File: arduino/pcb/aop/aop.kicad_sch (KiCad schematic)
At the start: 11 parts, among them J1 Conn_01x02_Pin, Q1 AO4435, SW1 SW_Push, SW2 SW_Push, U1 ESP32-C3_SUPERMINI_TH

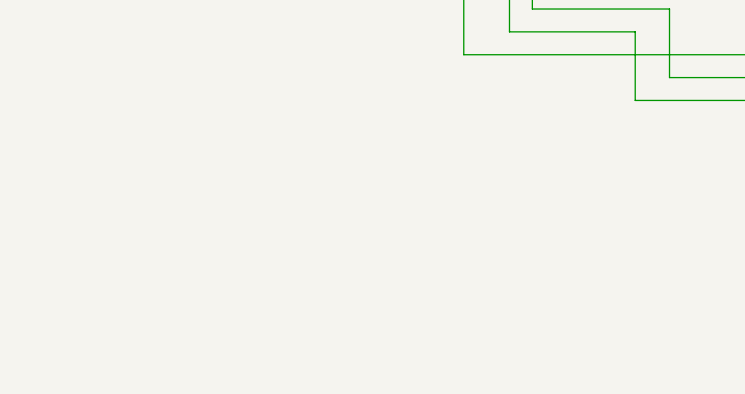
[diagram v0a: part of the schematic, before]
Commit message: [pcb] Stabilize power rail with capacitors
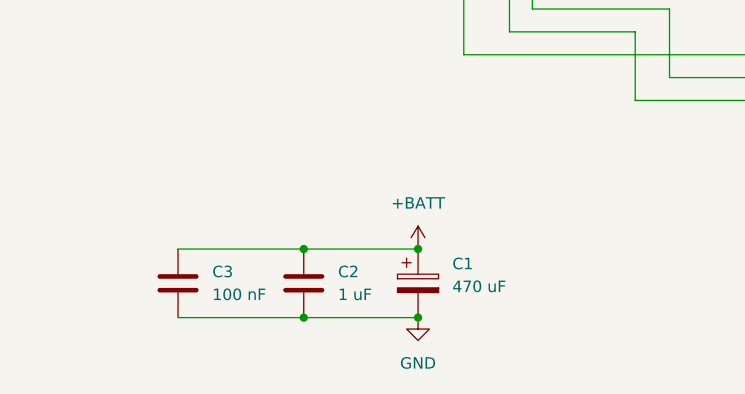
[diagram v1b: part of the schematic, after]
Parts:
- added C1: 470 uF, Capacitor_THT:CP_Radial_D8.0mm_P3.50mm, symbol Device:C_Polarized
- added C2: 1 uF, Capacitor_SMD:C_1206_3216Metric, symbol Device:C
- added C3: 100 nF, Capacitor_SMD:C_1206_3216Metric, symbol Device:C
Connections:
- net +BATT: now also C1.1, C2.1, C3.1
- net GND: now also C1.2, C2.2, C3.2

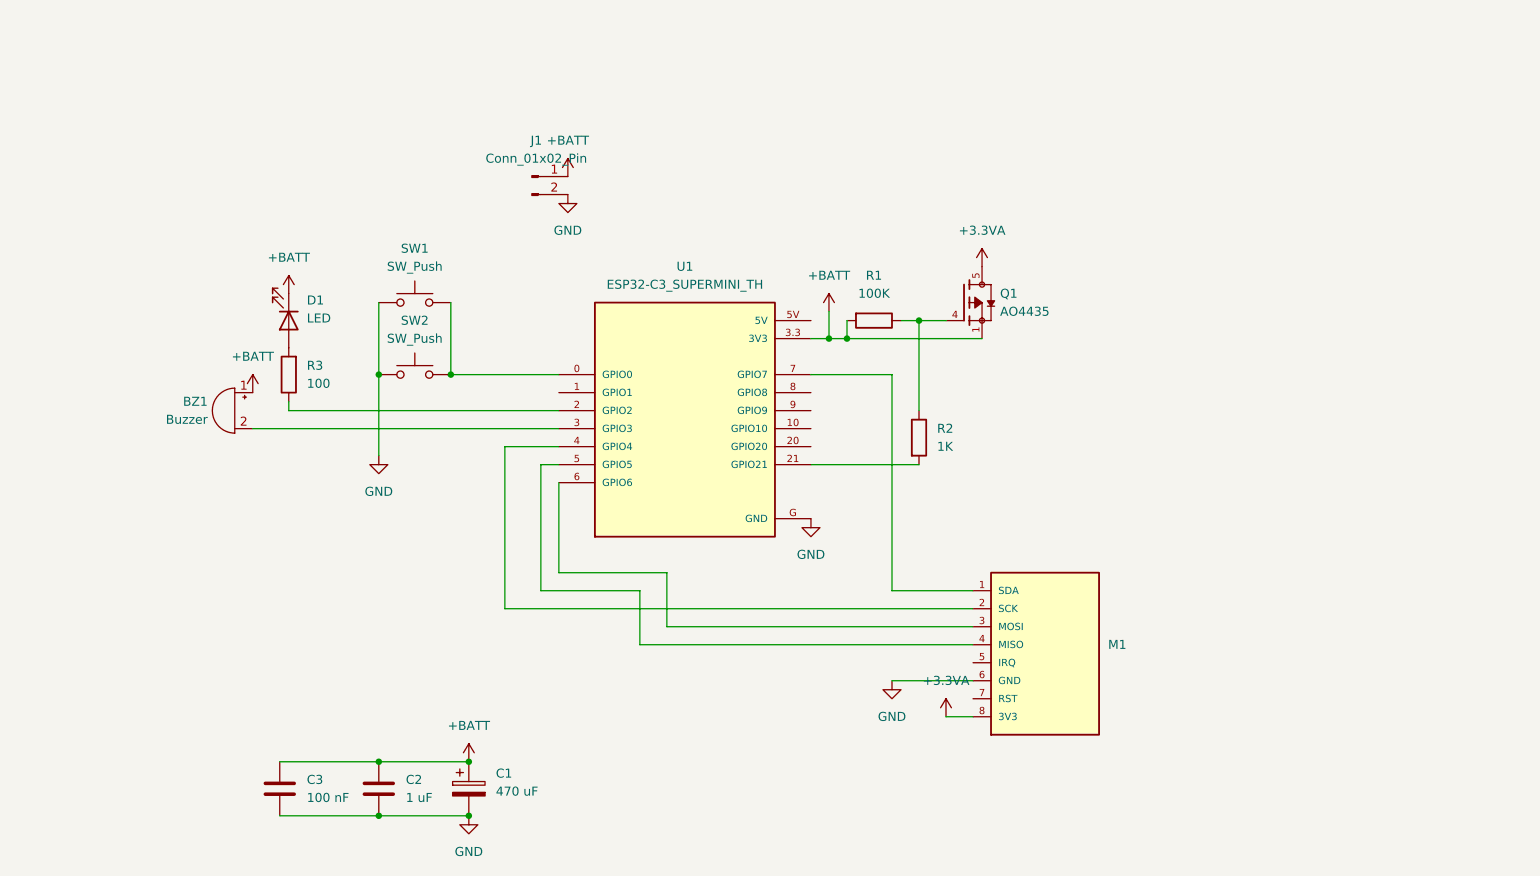
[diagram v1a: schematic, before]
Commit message: [pcb] Add DS3231
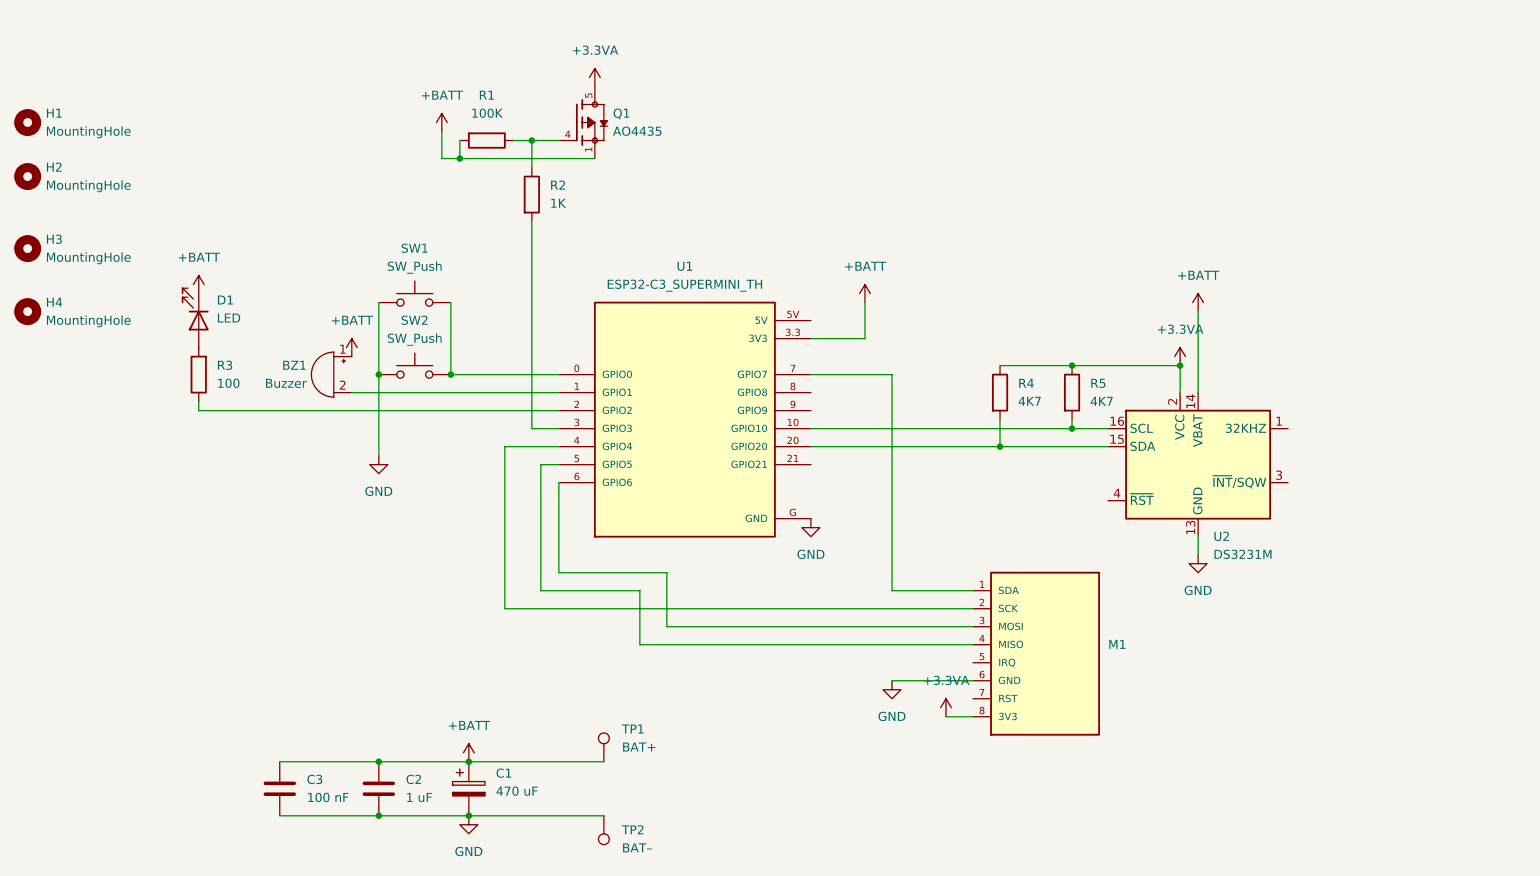
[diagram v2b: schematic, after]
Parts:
- removed J1: Conn_01x02_Pin, Connector_JST:JST_XH_B2B-XH-A_1x02_P2.50mm_Vertical, symbol Connector:Conn_01x02_Pin
- added H1, H2, H3, H4: MountingHole, MountingHole:MountingHole_2.2mm_M2, symbol Mechanical:MountingHole
- added R4, R5: 4K7, Resistor_SMD:R_1206_3216Metric, symbol Device:R
- added TP1: BAT+, TestPoint:TestPoint_THTPad_4.0x4.0mm_Drill2.0mm, symbol Connector:TestPoint
- added TP2: BAT–, TestPoint:TestPoint_THTPad_4.0x4.0mm_Drill2.0mm, symbol Connector:TestPoint
- added U2: DS3231M, Package_SO:SOIC-16W_7.5x10.3mm_P1.27mm, symbol Timer_RTC:DS3231M
- SW2: footprint Resistor_THT:R_Axial_DIN0414_L11.9mm_D4.5mm_P15.24mm_Horizontal -> Resistor_THT:R_Axial_DIN0207_L6.3mm_D2.5mm_P15.24mm_Horizontal
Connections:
- net +3.3VA: now also R4.1, R5.1, U2.2 (VCC)
- net +BATT: now also TP1.1, U2.14 (VBAT)
- net GND: now also TP2.1, U2.10 (GND), U2.11 (GND), U2.12 (GND), U2.13 (GND), U2.5 (GND), U2.6 (GND), U2.7 (GND), U2.8 (GND), U2.9 (GND)
- net at U1.1 (GPIO1): now also BZ1.2 (-)
- net at U1.10 (GPIO10): now also R5.2, U2.16 (SCL)
- net at U1.20 (GPIO20): now also R4.2, U2.15 (SDA)
- net at U1.21 (GPIO21): no longer R2.2
- net at U1.3 (GPIO3): now also R2.2; no longer BZ1.2 (-)
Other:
- moved on the sheet: BZ1, D1, Q1, R1, R2, R3

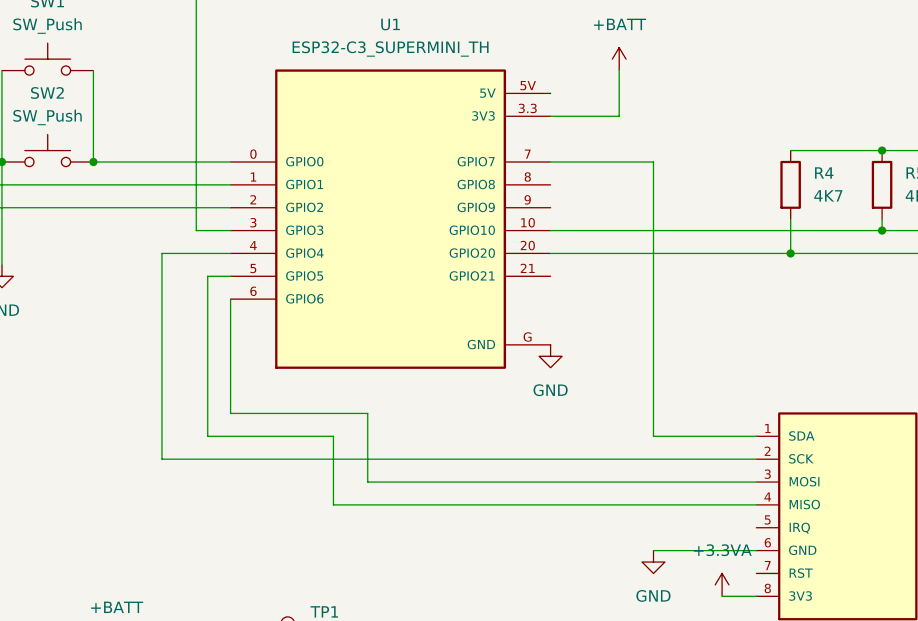
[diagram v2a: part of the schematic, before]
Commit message: [pcb] Choose closer pins for SPI
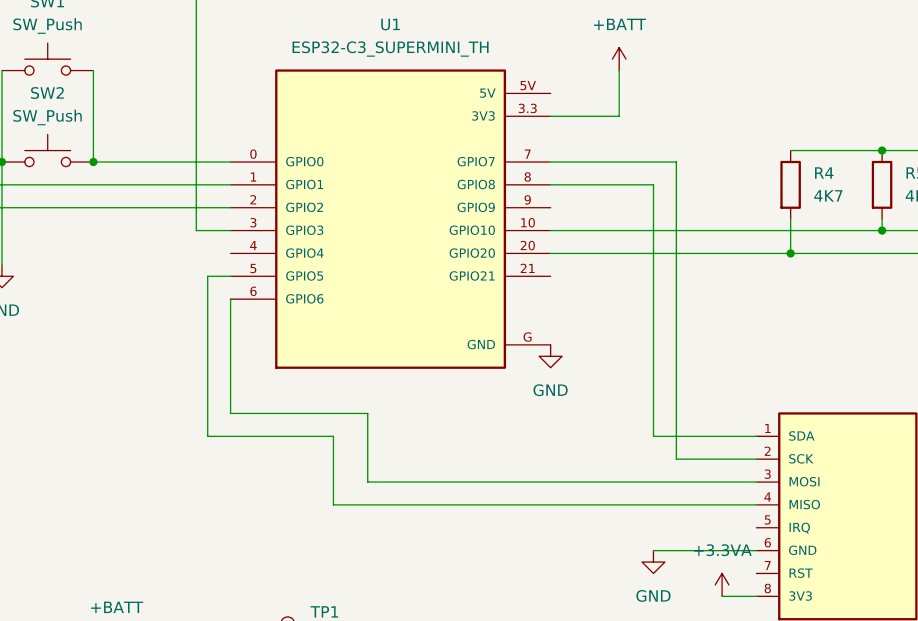
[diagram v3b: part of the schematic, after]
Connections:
- net at U1.4 (GPIO4): no longer M1.2 (SCK)
- net at U1.7 (GPIO7): now also M1.2 (SCK); no longer M1.1 (SDA)
- net at U1.8 (GPIO8): now also M1.1 (SDA)
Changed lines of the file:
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@@
+	(wire
+		(pts
+			(xy 168.91 114.3) (xy 168.91 86.36)
+		)
+		(stroke
+			(width 0)
+			(type default)
+		)
+	)
 	(wire
 		(pts
@@
 	(wire
 		(pts
+			(xy 171.45 116.84) (xy 171.45 83.82)
+		)
+		(stroke
+			(width 0)
+			(type default)
+		)
+	)
+	(wire
+		(pts
 			(xy 133.35 114.3) (xy 119.38 114.3)
 		)
@@
 	(wire
 		(pts
-			(xy 114.3 93.98) (xy 121.92 93.98)
-		)
-		(stroke
-			(width 0)
-			(type default)
-		)
-	)
-	(wire
-		(pts
 			(xy 212.09 106.68) (xy 212.09 109.22)
 		)
@@
 	(wire
 		(pts
-			(xy 180.34 116.84) (xy 114.3 116.84)
-		)
-		(stroke
-			(width 0)
-			(type default)
-		)
-	)
-	(wire
-		(pts
-			(xy 114.3 116.84) (xy 114.3 93.98)
-		)
-		(stroke
-			(width 0)
-			(type default)
-		)
-	)
-	(wire
-		(pts
 			(xy 180.34 119.38) (xy 137.16 119.38)
 		)
@@
 	(wire
 		(pts
+			(xy 180.34 116.84) (xy 171.45 116.84)
+		)
+		(stroke
+			(width 0)
+			(type default)
+		)
+	)
+	(wire
+		(pts
 			(xy 96.52 138.43) (xy 109.22 138.43)
 		)
@@
 	(wire
 		(pts
+			(xy 171.45 83.82) (xy 157.48 83.82)
+		)
+		(stroke
+			(width 0)
+			(type default)
+		)
+	)
+	(wire
+		(pts
 			(xy 209.55 82.55) (xy 209.55 86.36)
 		)
@@
 	(wire
 		(pts
-			(xy 168.91 83.82) (xy 157.48 83.82)
-		)
-		(stroke
-			(width 0)
-			(type default)
-		)
-	)
-	(wire
-		(pts
 			(xy 180.34 121.92) (xy 133.35 121.92)
 		)
@@
 	(wire
 		(pts
+			(xy 168.91 86.36) (xy 157.48 86.36)
+		)
+		(stroke
+			(width 0)
+			(type default)
+		)
+	)
+	(wire
+		(pts
 			(xy 106.68 73.66) (xy 106.68 83.82)
 		)
@@
 		)
 		(stroke
-			(width 0)
-			(type default)
-		)
-	)
-	(wire
-		(pts
-			(xy 168.91 114.3) (xy 168.91 83.82)
-		)
-		(stroke

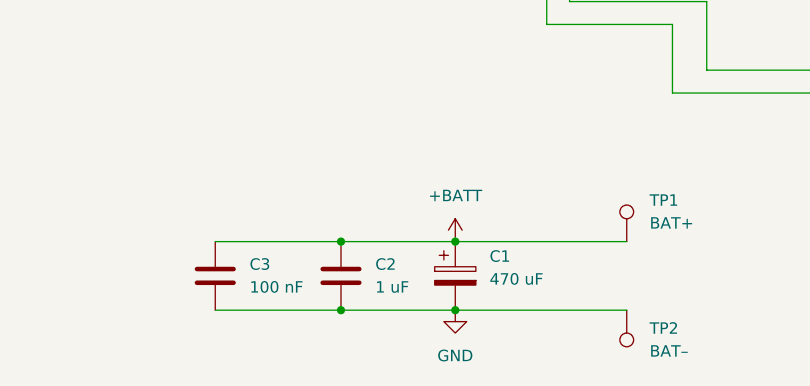
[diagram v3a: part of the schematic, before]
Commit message: [pcb] Reroute to improve ground plane continuity
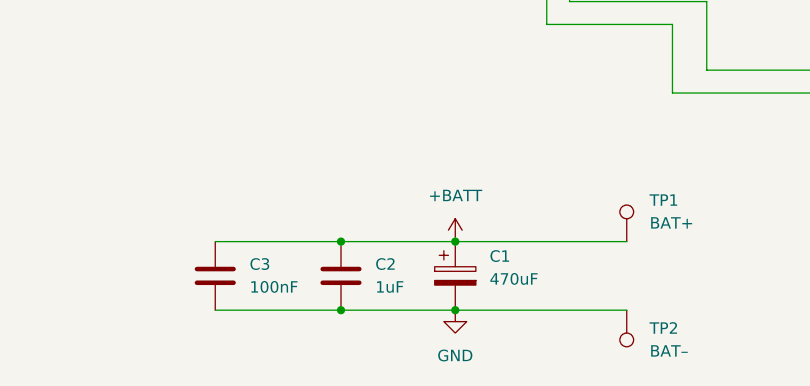
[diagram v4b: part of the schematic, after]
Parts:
- C1: value 470 uF -> 470uF
- C2: value 1 uF -> 1uF
- C3: value 100 nF -> 100nF
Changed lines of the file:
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@@
 			)
 		)
-		(property "Value" "1 uF"
+		(property "Value" "1uF"
 			(at 100.33 143.5099 0)
 			(show_name no)
@@
 			)
 		)
-		(property "Value" "100 nF"
+		(property "Value" "100nF"
 			(at 86.36 143.5099 0)
 			(show_name no)
@@
 			)
 		)
-		(property "Value" "470 uF"
+		(property "Value" "470uF"
 			(at 113.03 142.6209 0)
 			(show_name no)

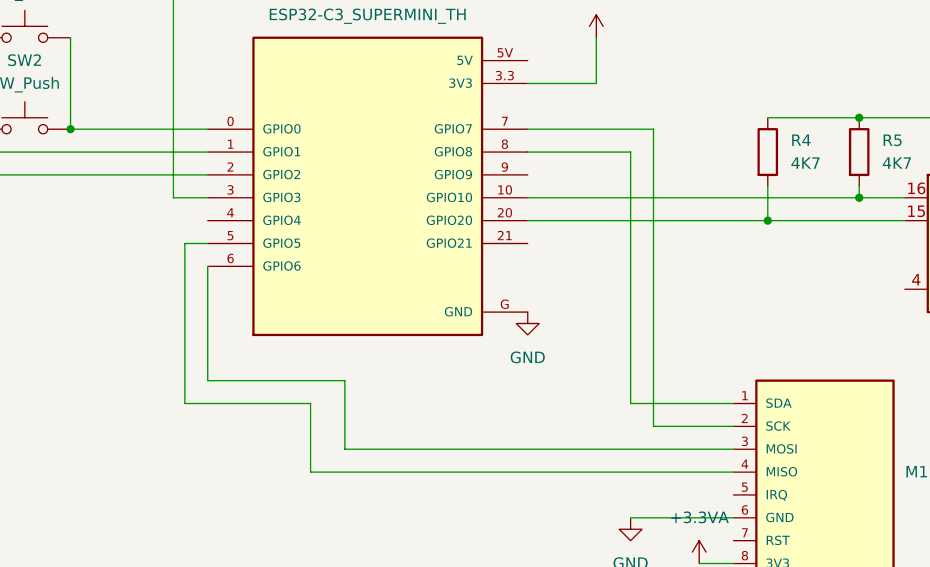
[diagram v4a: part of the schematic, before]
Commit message: [pcb] Move SDA to GPIO4 to avoid clash with UART
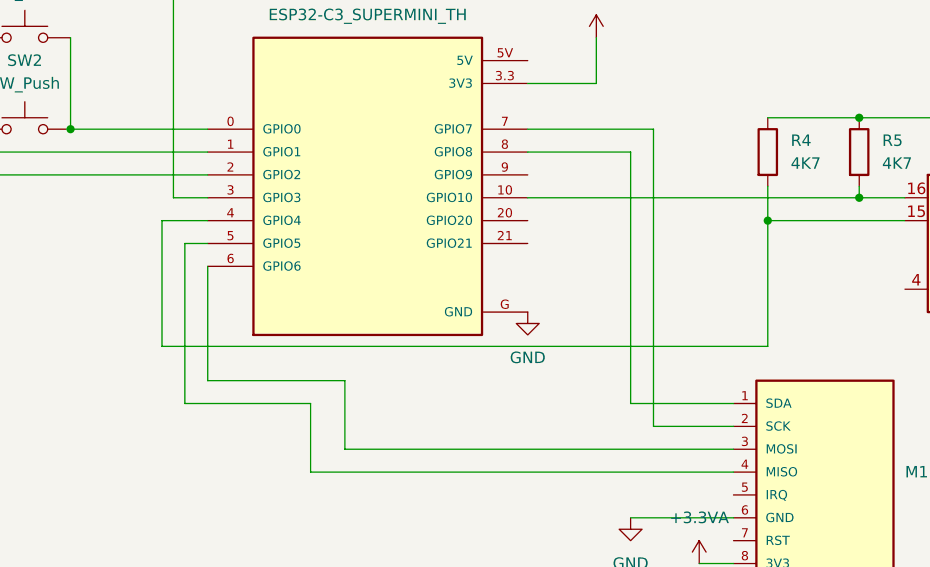
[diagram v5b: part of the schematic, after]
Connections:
- net at R4.2, U2.15 (SDA): now also U1.4 (GPIO4); no longer U1.20 (GPIO20)
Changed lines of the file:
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@@
 	(title_block
 		(title "AOP")
-		(rev "v0.4")
+		(rev "v0.5")
 	)
 	(junction
@@
 	)
 	(junction
+		(at 96.52 146.05)
+		(diameter 0)
+		(color 0 0 0 0)
+	)
+	(junction
+		(at 96.52 83.82)
+		(diameter 0)
+		(color 0 0 0 0)
+	)
+	(junction
+		(at 194.31 82.55)
+		(diameter 0)
+		(color 0 0 0 0)
+	)
+	(junction
 		(at 184.15 93.98)
 		(diameter 0)
@@
 	)
 	(junction
-		(at 96.52 146.05)
-		(diameter 0)
-		(color 0 0 0 0)
-	)
-	(junction
-		(at 96.52 83.82)
-		(diameter 0)
-		(color 0 0 0 0)
-	)
-	(junction
-		(at 194.31 82.55)
-		(diameter 0)
-		(color 0 0 0 0)
-	)
-	(junction
 		(at 107.95 53.34)
 		(diameter 0)
@@
 	(wire
 		(pts
+			(xy 116.84 107.95) (xy 184.15 107.95)
+		)
+		(stroke
+			(width 0)
+			(type default)
+		)
+	)
+	(wire
+		(pts
 			(xy 180.34 119.38) (xy 137.16 119.38)
 		)
@@
 	(wire
 		(pts
+			(xy 121.92 93.98) (xy 116.84 93.98)
+		)
+		(stroke
+			(width 0)
+			(type default)
+		)
+	)
+	(wire
+		(pts
 			(xy 121.92 91.44) (xy 118.11 91.44)
 		)
@@
 	(wire
 		(pts
-			(xy 157.48 93.98) (xy 184.15 93.98)
-		)
-		(stroke
-			(width 0)
-			(type default)
-		)
-	)
-	(wire
-		(pts
 			(xy 121.92 111.76) (xy 121.92 99.06)
 		)
@@
 	(wire
 		(pts
+			(xy 184.15 107.95) (xy 184.15 93.98)
+		)
+		(stroke
+			(width 0)
+			(type default)
+		)
+	)
+	(wire
+		(pts
 			(xy 92.71 86.36) (xy 121.92 86.36)
 		)
@@
 		)
 		(stroke
+			(width 0)
+			(type default)
+		)
+	)
+	(wire
+		(pts
+			(xy 116.84 93.98) (xy 116.84 107.95)
+		)
+		(stroke

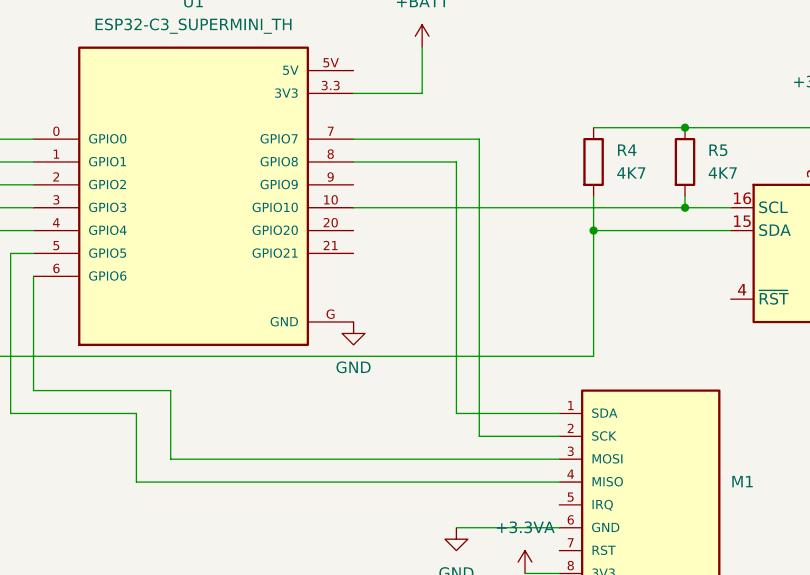
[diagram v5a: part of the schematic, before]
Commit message: [pcb] Use GPIO20 for SPI_SS because GPIO8 is high in the deep sleep
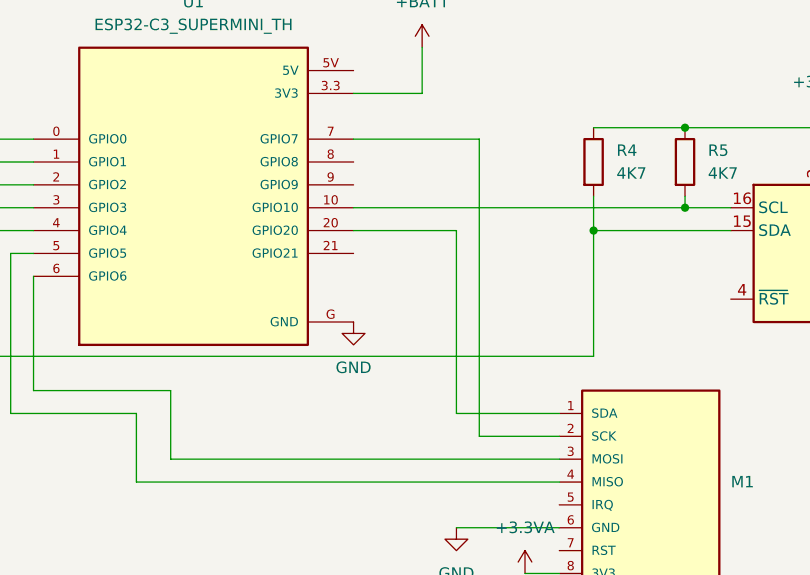
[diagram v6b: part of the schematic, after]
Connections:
- net at U1.20 (GPIO20): now also M1.1 (SDA)
- net at U1.8 (GPIO8): no longer M1.1 (SDA)
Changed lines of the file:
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@@
-	(wire
-		(pts
-			(xy 168.91 114.3) (xy 168.91 86.36)
-		)
-		(stroke
-			(width 0)
-			(type default)
-		)
-	)
 	(wire
 		(pts
@@
 	(wire
 		(pts
+			(xy 157.48 93.98) (xy 168.91 93.98)
+		)
+		(stroke
+			(width 0)
+			(type default)
+		)
+	)
+	(wire
+		(pts
 			(xy 121.92 88.9) (xy 71.12 88.9)
 		)
@@
 	(wire
 		(pts
+			(xy 168.91 93.98) (xy 168.91 114.3)
+		)
+		(stroke
+			(width 0)
+			(type default)
+		)
+	)
+	(wire
+		(pts
 			(xy 212.09 106.68) (xy 212.09 109.22)
 		)
@@
 		)
 		(stroke
-			(width 0)
-			(type default)
-		)
-	)
-	(wire
-		(pts
-			(xy 168.91 86.36) (xy 157.48 86.36)
-		)
-		(stroke
